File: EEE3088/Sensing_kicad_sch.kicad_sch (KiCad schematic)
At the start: 6 parts, among them U2 LTR-303ALS-01, U3 LTR-303ALS-01

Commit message: First night - c
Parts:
- added C1, C2: 1uF, symbol Device:C
- added R10, R5, R6, R7, R8, R9: 10K, symbol Device:R
- added R11, R12, R13, R14, R15, R16: 0, symbol Device:R
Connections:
- net at R2.1: now also R1.2, R16.2
- net GND: now reaches R2.2
- net GND: now also R4.2, U2.3 (GND), U3.3 (GND), C1.2, C2.2
- net at R4.1: now also R3.2, R15.1
- net +3.3V: now reaches R1.1
- net +3.3V: now also R3.1, U2.1 (VDD), U3.1 (VDD), C1.1, C2.1, R10.1, R5.1, R6.1, R7.1, R8.1, R9.1
- net at U2.4 (SCL): now also R14.2, R8.2
- net at U2.5 (INT): now also R10.2
- net at U2.6 (SDA): now also R13.2, R9.2
- net at U3.4 (SCL): now also R12.2, R5.2
- net at U3.5 (INT): now also R7.2
- net at U3.6 (SDA): now also R11.1, R6.2
- new net LDR_Vout: R15.2
- new net LDR_Vout-A: R16.1
- new net SCL_ALS: R12.1
- new net SCL_ALS-A: R14.1
- new net SDA_ALS: R11.2
- new net SDA_ALS-A: R13.1
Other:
- moved on the sheet: R1, R2, R3, R4, U2, U3

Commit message: 05/03
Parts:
- added TP1, TP2, TP3, TP4, TP5, TP6, TP7: TestPoint, symbol Connector:TestPoint
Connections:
- net +3.3V: now also TP3.1
- net SCL_ALS: now also TP6.1
- net SCL_ALS-A: now also TP4.1
- net at R1.2, R16.2, R2.1: now also TP2.1
- net at R15.1, R3.2, R4.1: now also TP1.1
- net at R11.1, R6.2, U3.6 (SDA): now also TP7.1
- net at R13.2, R9.2, U2.6 (SDA): now also TP5.1
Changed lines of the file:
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@@
   (junction (at 196.85 48.26) (diameter 0) (color 0 0 0 0)
   )
+  (junction (at 165.1 106.68) (diameter 0) (color 0 0 0 0)
+  )
+  (junction (at 177.8 48.26) (diameter 0) (color 0 0 0 0)
+  )
   (junction (at 184.15 53.34) (diameter 0) (color 0 0 0 0)
   )
+  (junction (at 252.73 38.1) (diameter 0) (color 0 0 0 0)
+  )
   (junction (at 180.34 106.68) (diameter 0) (color 0 0 0 0)
   )
+  (junction (at 176.53 101.6) (diameter 0) (color 0 0 0 0)
+  )
+  (junction (at 83.82 104.14) (diameter 0) (color 0 0 0 0)
+  )
   (junction (at 101.6 48.26) (diameter 0) (color 0 0 0 0)
   )
@@
   (junction (at 194.31 101.6) (diameter 0) (color 0 0 0 0)
   )
+  (junction (at 162.56 53.34) (diameter 0) (color 0 0 0 0)
+  )
+  (junction (at 77.47 48.26) (diameter 0) (color 0 0 0 0)
+  )
   (wire (pts (xy 213.36 60.96) (xy 213.36 67.31))
     (stroke (width 0) (type default))
@@
     (stroke (width 0) (type default))
   )
-  (wire (pts (xy 162.56 106.68) (xy 167.64 106.68))
+  (wire (pts (xy 162.56 106.68) (xy 165.1 106.68))
+    (stroke (width 0) (type default))
+  )
+  (wire (pts (xy 77.47 48.26) (xy 101.6 48.26))
     (stroke (width 0) (type default))
   )
@@
     (stroke (width 0) (type default))
   )
+  (wire (pts (xy 165.1 106.68) (xy 167.64 106.68))
+    (stroke (width 0) (type default))
+  )
   (wire (pts (xy 194.31 80.01) (xy 194.31 85.09))
     (stroke (width 0) (type default))
@@
     (stroke (width 0) (type default))
   )
+  (wire (pts (xy 252.73 38.1) (xy 252.73 40.64))
+    (stroke (width 0) (type default))
+  )
   (wire (pts (xy 232.41 50.8) (xy 223.52 50.8))
     (stroke (width 0) (type default))
@@
     (stroke (width 0) (type default))
   )
+  (wire (pts (xy 162.56 53.34) (xy 166.37 53.34))
+    (stroke (width 0) (type default))
+  )
   (wire (pts (xy 102.87 88.9) (xy 102.87 93.98))
     (stroke (width 0) (type default))
@@
     (stroke (width 0) (type default))
   )
-  (wire (pts (xy 66.04 48.26) (xy 101.6 48.26))
+  (wire (pts (xy 66.04 48.26) (xy 77.47 48.26))
     (stroke (width 0) (type default))
   )
@@
     (stroke (width 0) (type default))
   )
-  (wire (pts (xy 252.73 35.56) (xy 252.73 40.64))
+  (wire (pts (xy 252.73 35.56) (xy 252.73 38.1))
+    (stroke (width 0) (type default))
+  )
+  (wire (pts (xy 177.8 48.26) (xy 196.85 48.26))
     (stroke (width 0) (type default))
   )
@@
     (stroke (width 0) (type default))
   )
-  (wire (pts (xy 69.85 104.14) (xy 102.87 104.14))
-    (stroke (width 0) (type default))
-  )
-  (wire (pts (xy 158.75 53.34) (xy 166.37 53.34))
+  (wire (pts (xy 69.85 104.14) (xy 83.82 104.14))
+    (stroke (width 0) (type default))
+  )
+  (wire (pts (xy 158.75 53.34) (xy 162.56 53.34))
     (stroke (width 0) (type default))
   )
@@
     (stroke (width 0) (type default))
   )
-  (wire (pts (xy 175.26 101.6) (xy 194.31 101.6))
-    (stroke (width 0) (type default))
-  )
-  (wire (pts (xy 173.99 48.26) (xy 196.85 48.26))
+  (wire (pts (xy 175.26 101.6) (xy 176.53 101.6))
+    (stroke (width 0) (type default))
+  )
+  (wire (pts (xy 83.82 104.14) (xy 102.87 104.14))
+    (stroke (width 0) (type default))
+  )
+  (wire (pts (xy 173.99 48.26) (xy 177.8 48.26))
     (stroke (width 0) (type default))
   )
@@
   )
   (wire (pts (xy 101.6 48.26) (xy 101.6 49.53))
+    (stroke (width 0) (type default))
+  )
+  (wire (pts (xy 176.53 101.6) (xy 194.31 101.6))
     (stroke (width 0) (type default))
   )
@@
     )
   )
+  (symbol (lib_id "Connector:TestPoint") (at 177.8 48.26 0) (unit 1)
+    (in_bom yes) (on_board yes) (dnp no) (fields_autoplaced)
+    (property "Reference" "TP5" (at 180.34 44.323 0)
+      (effects (font (size 1.27 1.27)) (justify left))
+    )
+    (property "Value" "TestPoint" (at 180.34 46.863 0)
+      (effects (font (size 1.27 1.27)) (justify left))
+    )
+    (property "Footprint" "" (at 182.88 48.26 0)
+      (effects (font (size 1.27 1.27)) hide)
+    )
+    (property "Datasheet" "~" (at 182.88 48.26 0)
+      (effects (font (size 1.27 1.27)) hide)
+    )
+    (pin "1")
+    (instances
+      (project "EEE3088"
+        (path "/83bdd5e1-981a-4ca1-9a2f-70dea9f00850/d16a673b-d677-4a4a-a11c-ee22bd422692"
+          (reference "TP5") (unit 1)
+        )
+      )
+    )
+  )
   (symbol (lib_id "Device:R") (at 184.15 35.56 0) (unit 1)
     (in_bom yes) (on_board yes) (dnp no) (fields_autoplaced)
@@
     )
   )
+  (symbol (lib_id "Connector:TestPoint") (at 165.1 106.68 0) (unit 1)
+    (in_bom yes) (on_board yes) (dnp no) (fields_autoplaced)
+    (property "Reference" "TP6" (at 167.64 102.743 0)
+      (effects (font (size 1.27 1.27)) (justify left))
+    )
+    (property "Value" "TestPoint" (at 167.64 105.283 0)
+      (effects (font (size 1.27 1.27)) (justify left))
+    )
+    (property "Footprint" "" (at 170.18 106.68 0)
+      (effects (font (size 1.27 1.27)) hide)
+    )
+    (property "Datasheet" "~" (at 170.18 106.68 0)
+      (effects (font (size 1.27 1.27)) hide)
+    )
+    (pin "1")
+    (instances
+      (project "EEE3088"
+        (path "/83bdd5e1-981a-4ca1-9a2f-70dea9f00850/d16a673b-d677-4a4a-a11c-ee22bd422692"
+          (reference "TP6") (unit 1)
+        )
+      )
+    )
+  )
   (symbol (lib_id "Device:R") (at 66.04 104.14 90) (unit 1)
     (in_bom yes) (on_board yes) (dnp no) (fields_autoplaced)
@@
     )
   )
+  (symbol (lib_id "Connector:TestPoint") (at 162.56 53.34 0) (unit 1)
+    (in_bom yes) (on_board yes) (dnp no) (fields_autoplaced)
+    (property "Reference" "TP4" (at 165.1 49.403 0)
+      (effects (font (size 1.27 1.27)) (justify left))
+    )
+    (property "Value" "TestPoint" (at 165.1 51.943 0)
+      (effects (font (size 1.27 1.27)) (justify left))
+    )
+    (property "Footprint" "" (at 167.64 53.34 0)
+      (effects (font (size 1.27 1.27)) hide)
+    )
+    (property "Datasheet" "~" (at 167.64 53.34 0)
+      (effects (font (size 1.27 1.27)) hide)
+    )
+    (pin "1")
+    (instances
+      (project "EEE3088"
+        (path "/83bdd5e1-981a-4ca1-9a2f-70dea9f00850/d16a673b-d677-4a4a-a11c-ee22bd422692"
+          (reference "TP4") (unit 1)
+        )
+      )
+    )
+  )
   (symbol (lib_id "power:+3.3V") (at 101.6 33.02 0) (unit 1)
     (in_bom yes) (on_board yes) (dnp no) (fields_autoplaced)
@@
         (path "/83bdd5e1-981a-4ca1-9a2f-70dea9f00850/d16a673b-d677-4a4a-a11c-ee22bd422692"
           (reference "C2") (unit 1)
+        )
+      )
+    )
+  )
+  (symbol (lib_id "Connector:TestPoint") (at 83.82 104.14 0) (unit 1)
+    (in_bom yes) (on_board yes) (dnp no) (fields_autoplaced)
+    (property "Reference" "TP2" (at 86.36 100.203 0)
+      (effects (font (size 1.27 1.27)) (justify left))
+    )
+    (property "Value" "TestPoint" (at 86.36 102.743 0)
+      (effects (font (size 1.27 1.27)) (justify left))
+    )
+    (property "Footprint" "" (at 88.9 104.14 0)
+      (effects (font (size 1.27 1.27)) hide)
+    )
+    (property "Datasheet" "~" (at 88.9 104.14 0)
+      (effects (font (size 1.27 1.27)) hide)
+    )
+    (pin "1")
+    (instances
+      (project "EEE3088"
+        (path "/83bdd5e1-981a-4ca1-9a2f-70dea9f00850/d16a673b-d677-4a4a-a11c-ee22bd422692"
+          (reference "TP2") (unit 1)
         )
       )
@@
     )
   )
+  (symbol (lib_id "Connector:TestPoint") (at 252.73 38.1 270) (unit 1)
+    (in_bom yes) (on_board yes) (dnp no) (fields_autoplaced)
+    (property "Reference" "TP3" (at 257.81 37.465 90)
+      (effects (font (size 1.27 1.27)) (justify left))
+    )
+    (property "Value" "TestPoint" (at 257.81 40.005 90)
+      (effects (font (size 1.27 1.27)) (justify left))
+    )
+    (property "Footprint" "" (at 252.73 43.18 0)
+      (effects (font (size 1.27 1.27)) hide)
+    )
+    (property "Datasheet" "~" (at 252.73 43.18 0)
+      (effects (font (size 1.27 1.27)) hide)
+    )
+    (pin "1")
+    (instances
+      (project "EEE3088"
+        (path "/83bdd5e1-981a-4ca1-9a2f-70dea9f00850/d16a673b-d677-4a4a-a11c-ee22bd422692"
+          (reference "TP3") (unit 1)
+        )
+      )
+    )
+  )
   (symbol (lib_id "Device:R") (at 170.18 48.26 90) (unit 1)
     (in_bom yes) (on_board yes) (dnp no)
@@
     )
   )
+  (symbol (lib_id "Connector:TestPoint") (at 77.47 48.26 0) (unit 1)
+    (in_bom yes) (on_board yes) (dnp no) (fields_autoplaced)
+    (property "Reference" "TP1" (at 80.01 44.323 0)
+      (effects (font (size 1.27 1.27)) (justify left))
+    )
+    (property "Value" "TestPoint" (at 80.01 46.863 0)
+      (effects (font (size 1.27 1.27)) (justify left))
+    )
+    (property "Footprint" "" (at 82.55 48.26 0)
+      (effects (font (size 1.27 1.27)) hide)
+    )
+    (property "Datasheet" "~" (at 82.55 48.26 0)
+      (effects (font (size 1.27 1.27)) hide)
+    )
+    (pin "1")
+    (instances
+      (project "EEE3088"
+        (path "/83bdd5e1-981a-4ca1-9a2f-70dea9f00850/d16a673b-d677-4a4a-a11c-ee22bd422692"
+          (reference "TP1") (unit 1)
+        )
+      )
+    )
+  )
   (symbol (lib_id "Device:R") (at 62.23 48.26 270) (unit 1)
     (in_bom yes) (on_board yes) (dnp no) (fields_autoplaced)
@@
         )
       )
+    )
+  )
+  (symbol (lib_id "Connector:TestPoint") (at 176.53 101.6 0) (unit 1)
+    (in_bom yes) (on_board yes) (dnp no) (fields_autoplaced)
+    (property "Reference" "TP7" (at 179.07 97.663 0)
+      (effects (font (size 1.27 1.27)) (justify left))
+    )
+    (property "Value" "TestPoint" (at 179.07 100.203 0)
+      (effects (font (size 1.27 1.27)) (justify left))
+    )
+    (property "Footprint" "" (at 181.61 101.6 0)
+      (effects (font (size 1.27 1.27)) hide)
+    )
+    (property "Datasheet" "~" (at 181.61 101.6 0)
+      (effects (font (size 1.27 1.27)) hide)
+    )
+    (pin "1")
+    (instances
+      (project "EEE3088"
+        (path "/83bdd5e1-981a-4ca1-9a2f-70dea9f00850/d16a673b-d677-4a4a-a11c-ee22bd422692"
+          (reference "TP7") (unit 1)
+        )
+      )

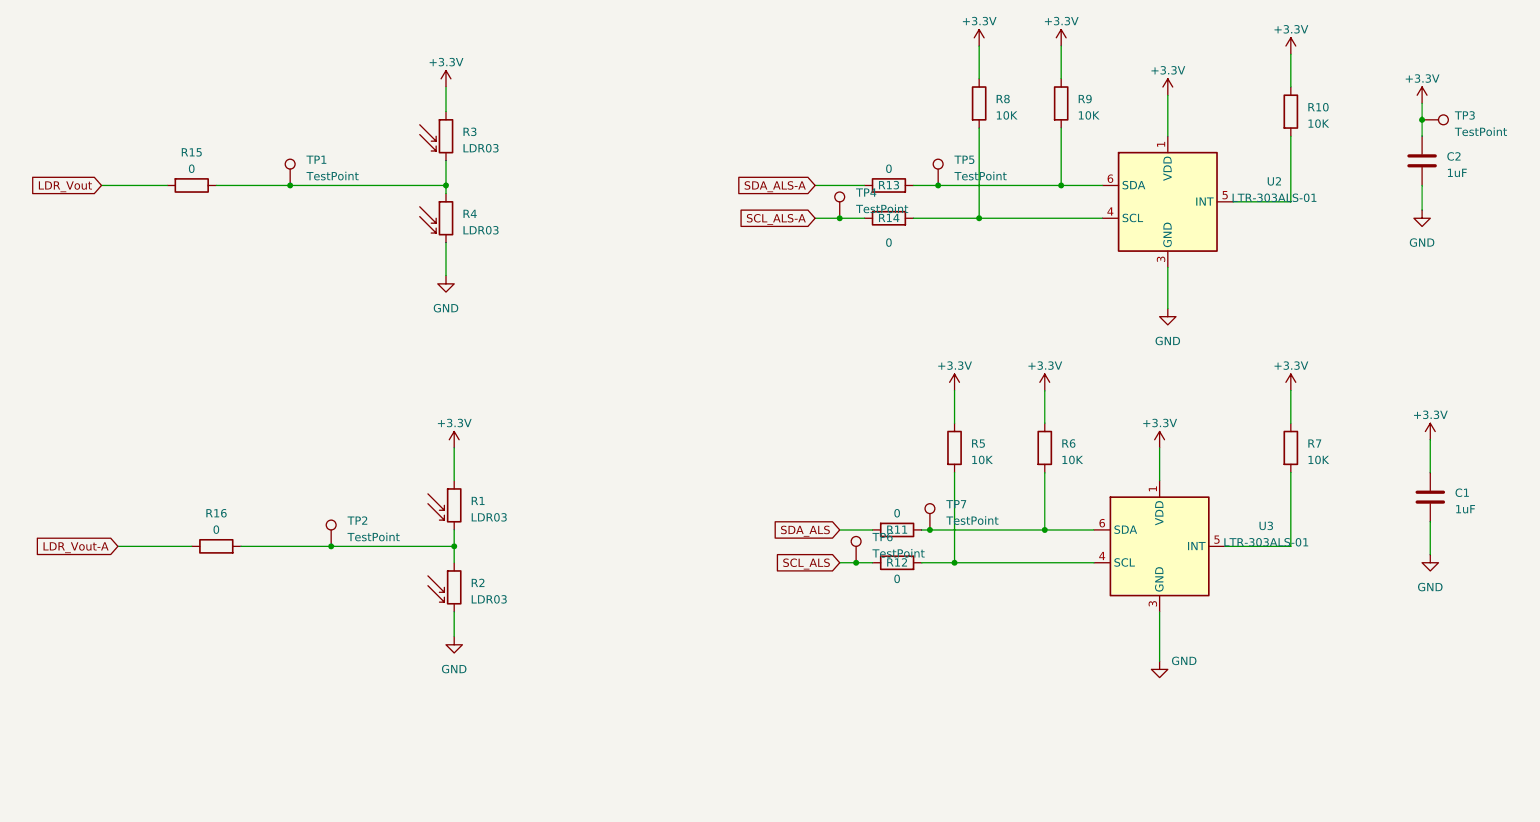
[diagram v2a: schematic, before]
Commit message: Proposal update
Power update
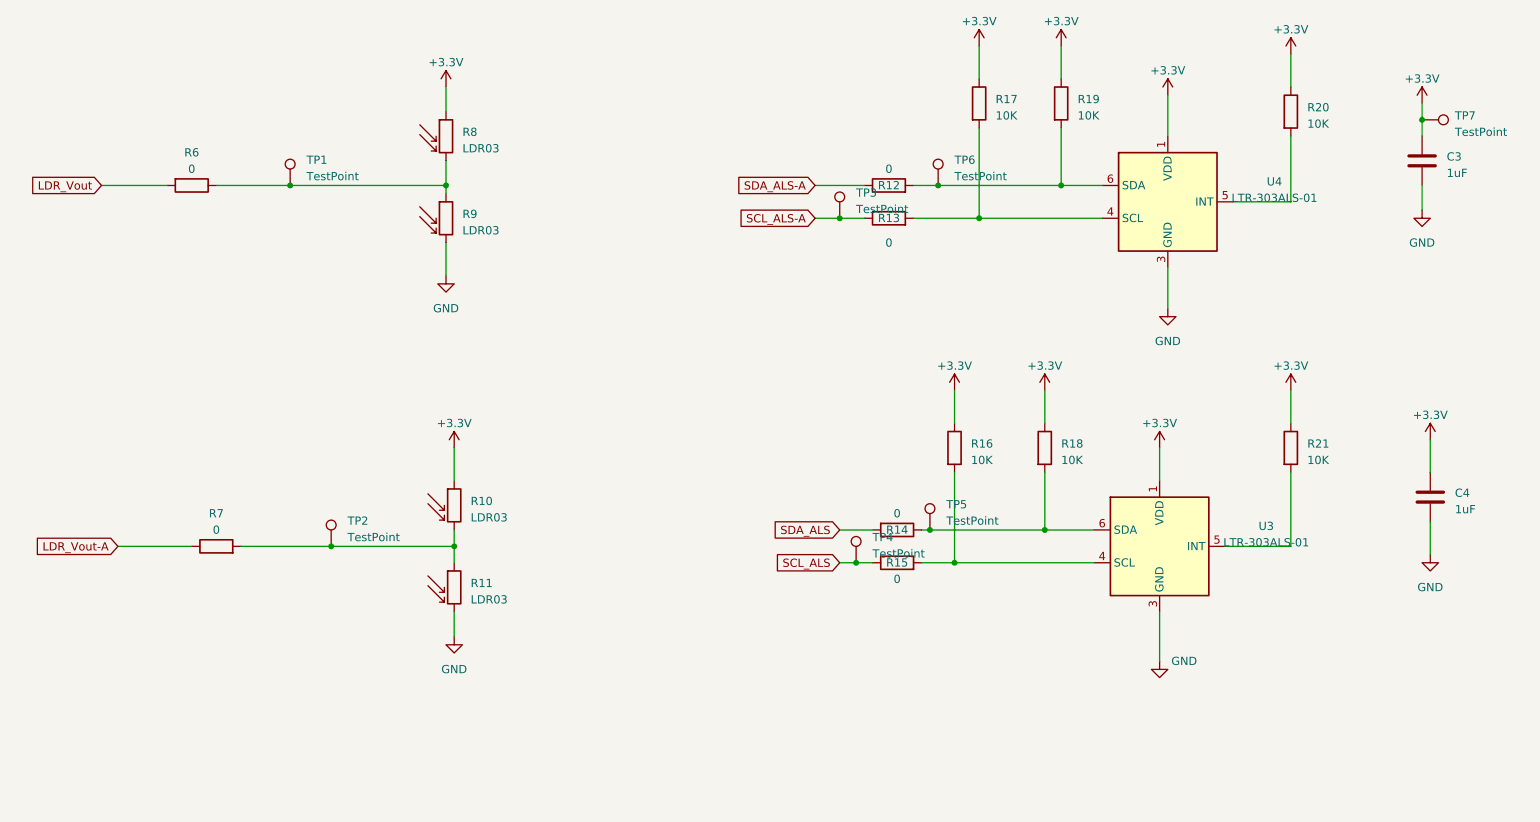
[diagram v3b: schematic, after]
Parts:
- renumbered C2 to C3, C1 to C4, R1 to R10, R2 to R11, R13 to R12, R14 to R13, R11 to R14, R12 to R15, R5 to R16, R8 to R17, R6 to R18, R9 to R19, R10 to R20, R7 to R21, R15 to R6, R16 to R7, R3 to R8, R4 to R9, TP4 to TP3, TP6 to TP4, TP7 to TP5, TP5 to TP6, TP3 to TP7, U2 to U4

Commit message: Power update
included Low voltage reg
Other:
- company: (none) -> UCT
